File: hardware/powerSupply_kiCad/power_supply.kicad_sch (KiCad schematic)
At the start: 23 parts, among them IC1 LT7101EUHE-PBF, J1 CLCK, J2 MODE

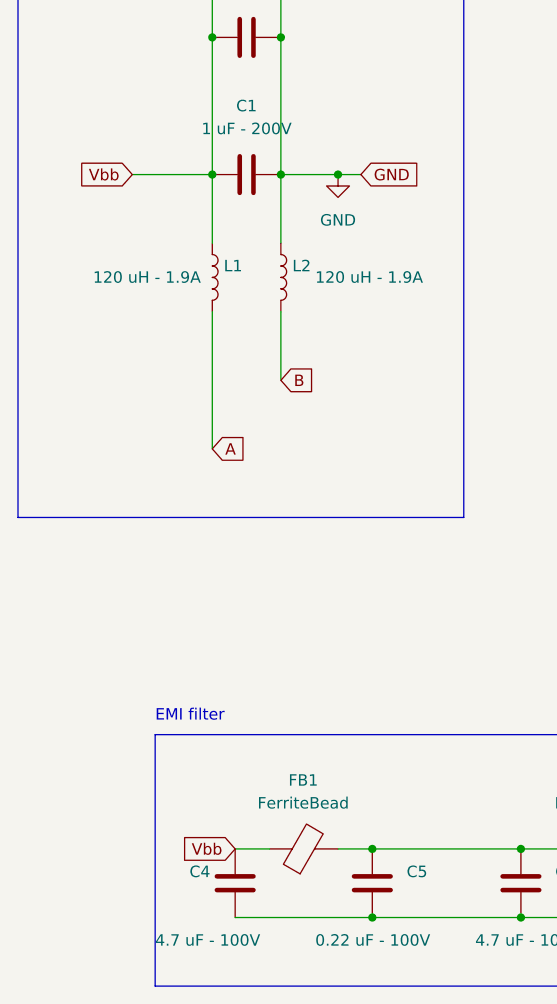
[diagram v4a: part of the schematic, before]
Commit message: Plane configuration
The Vin and Vbb are merged into a single net. Is the C1 to C3 usefull then? Must revise the decoupling strategy
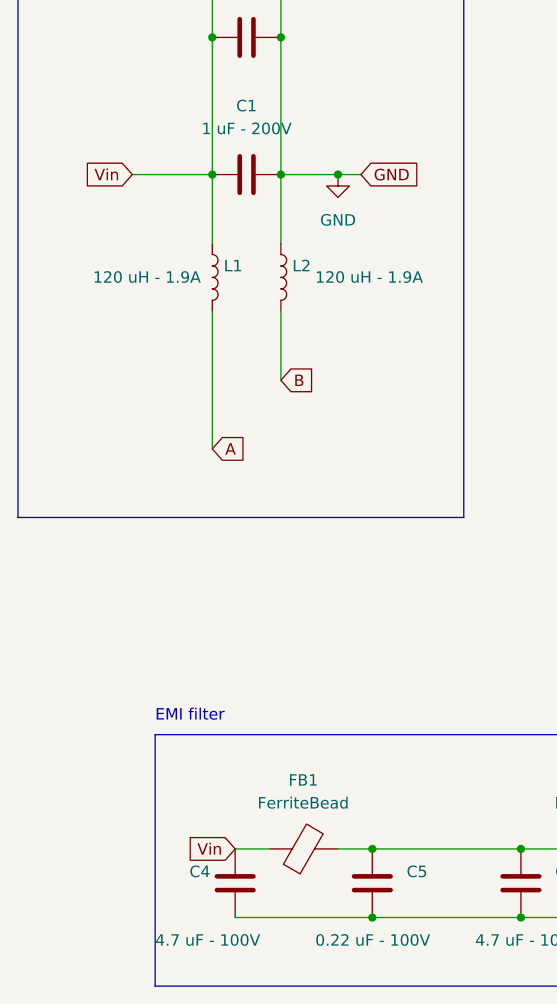
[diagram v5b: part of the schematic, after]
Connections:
- net Vbb is gone; now on net Vin: C1.1, C2.1, C3.1, C4.1, FB1.1, L1.1
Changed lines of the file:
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@@
     (effects (font (size 1.27 1.27)) (justify left bottom))
   )
-  (global_label "Vbb" (shape input) (at 53.34 154.94 180) (fields_autoplaced)
+  (global_label "Vin" (shape input) (at 53.34 154.94 180) (fields_autoplaced)
     (effects (font (size 1.27 1.27)) (justify right))
-    (property "Intersheet References" "${INTERSHEET_REFS}" (id 0) (at 47.5402 154.8606 0)
+    (property "Intersheet References" "${INTERSHEET_REFS}" (id 0) (at 48.0845 154.8606 0)
       (effects (font (size 1.27 1.27)) (justify right) hide)
     )
@@
     )
   )
-  (global_label "Vbb" (shape input) (at 41.91 80.01 180) (fields_autoplaced)
+  (global_label "Vin" (shape input) (at 41.91 80.01 180) (fields_autoplaced)
     (effects (font (size 1.27 1.27)) (justify right))
-    (property "Intersheet References" "${INTERSHEET_REFS}" (id 0) (at 36.1102 79.9306 0)
+    (property "Intersheet References" "${INTERSHEET_REFS}" (id 0) (at 36.6545 79.9306 0)
       (effects (font (size 1.27 1.27)) (justify right) hide)
     )

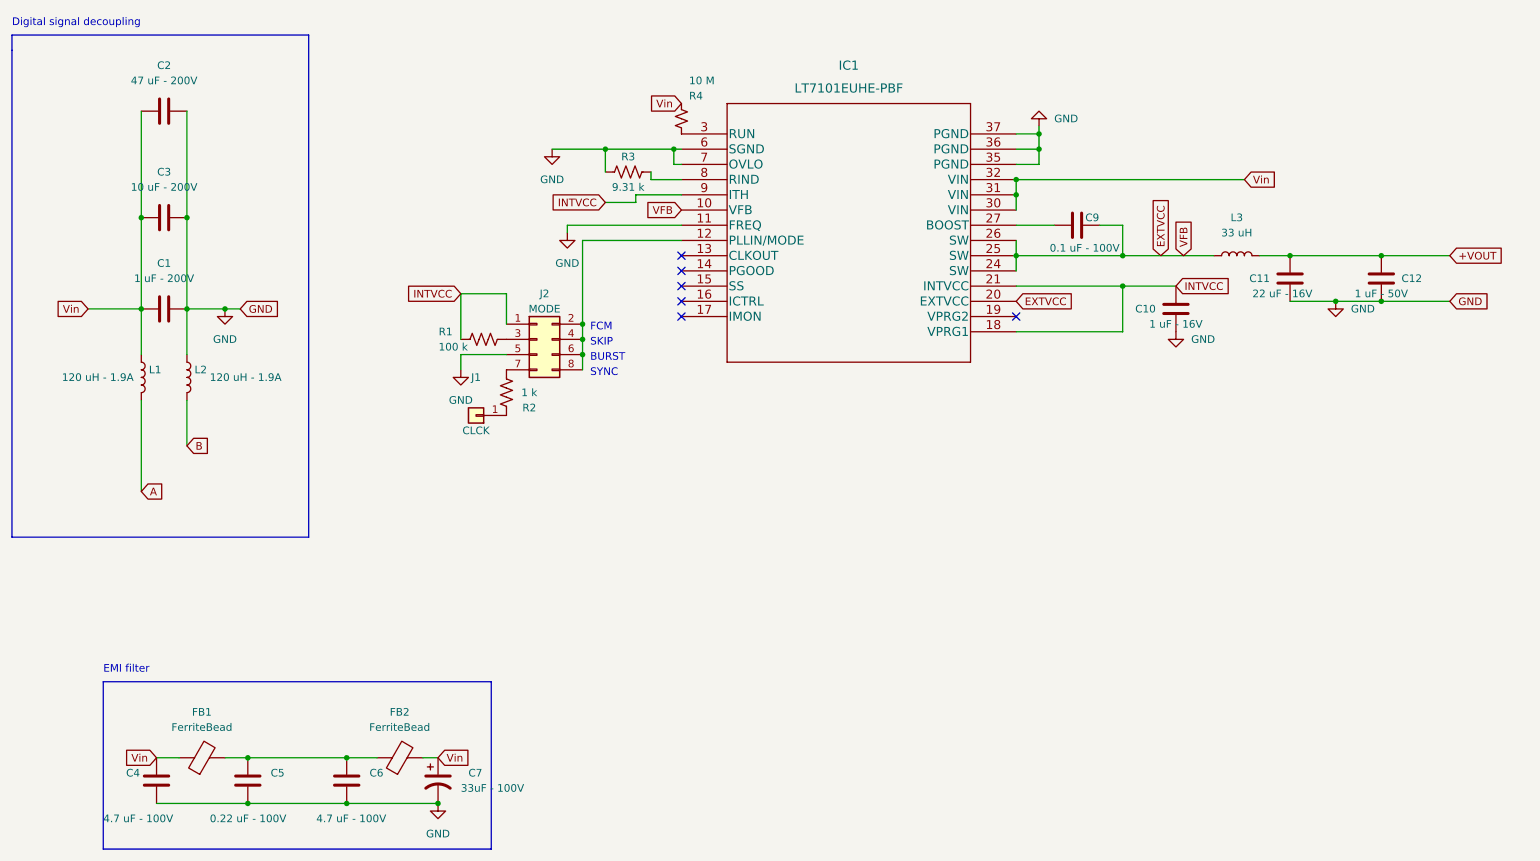
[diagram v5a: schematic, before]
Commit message: Finished connection and zone
The Vbb and Vin have returned to separate nets and zones. In this configuration the spike of volage when turning on the source at the surface will be handle by C1,C2 and C3.
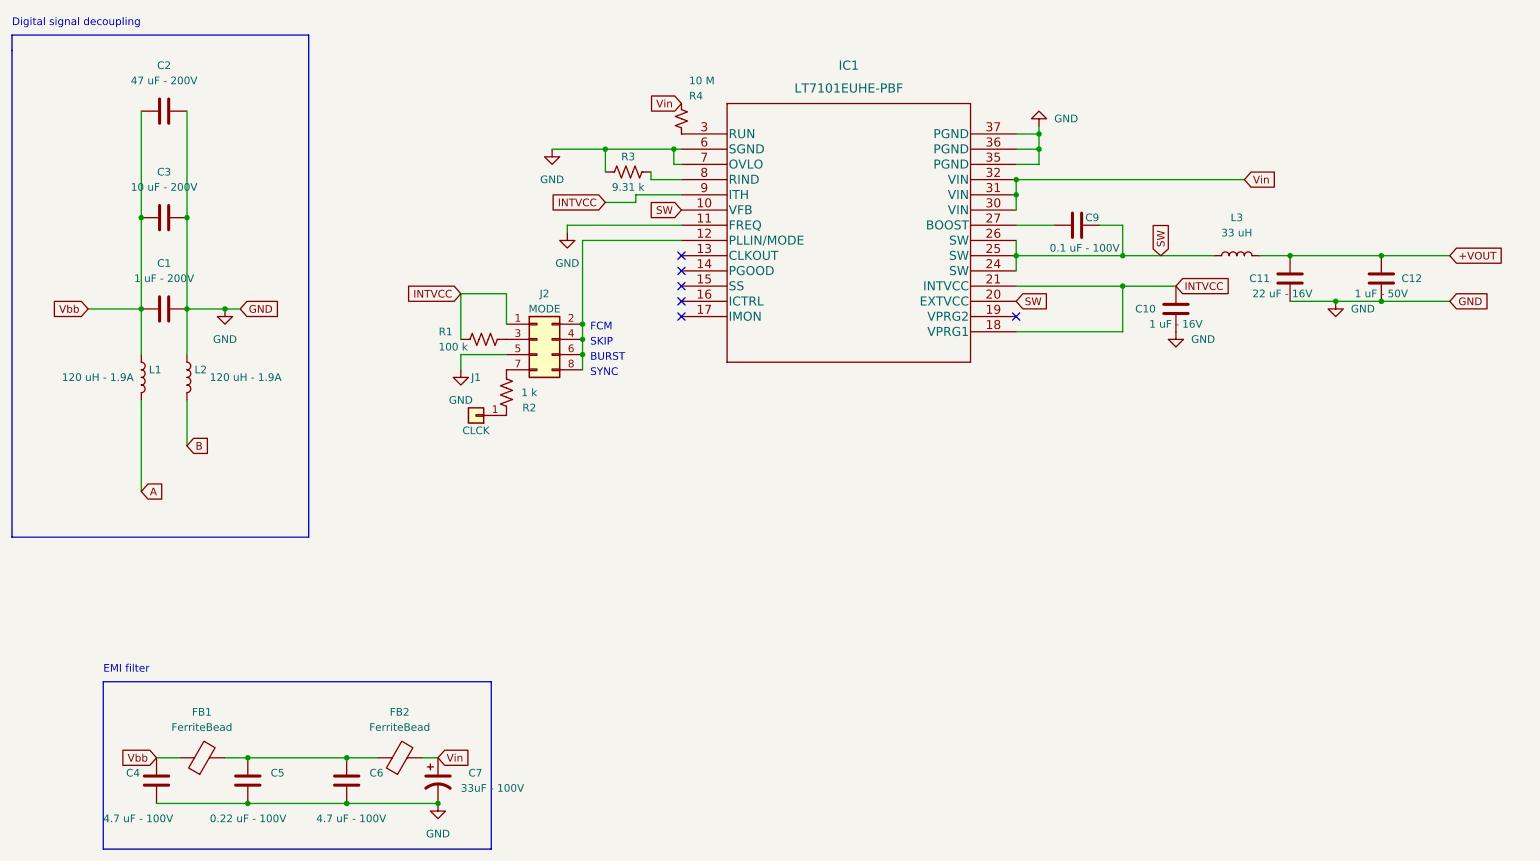
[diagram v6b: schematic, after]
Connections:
- net Vin: no longer C1.1, C2.1, C3.1, C4.1, FB1.1, L1.1
- net EXTVCC renamed SW
- new net Vbb: C1.1, C2.1, C3.1, C4.1, FB1.1, L1.1
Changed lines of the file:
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@@
     (effects (font (size 1.27 1.27)) (justify left bottom))
   )
-  (global_label "Vin" (shape input) (at 53.34 154.94 180) (fields_autoplaced)
+  (global_label "Vbb" (shape input) (at 53.34 154.94 180) (fields_autoplaced)
     (effects (font (size 1.27 1.27)) (justify right))
-    (property "Intersheet References" "${INTERSHEET_REFS}" (id 0) (at 48.0845 154.8606 0)
+    (property "Intersheet References" "${INTERSHEET_REFS}" (id 0) (at 47.5402 154.8606 0)
       (effects (font (size 1.27 1.27)) (justify right) hide)
     )
@@
     )
   )
-  (global_label "EXTVCC" (shape input) (at 196.85 78.74 0) (fields_autoplaced)
+  (global_label "SW" (shape input) (at 196.85 78.74 0) (fields_autoplaced)
     (effects (font (size 1.27 1.27)) (justify left))
-    (property "Intersheet References" "${INTERSHEET_REFS}" (id 0) (at 206.2179 78.6606 0)
+    (property "Intersheet References" "${INTERSHEET_REFS}" (id 0) (at 201.9241 78.6606 0)
       (effects (font (size 1.27 1.27)) (justify left) hide)
     )
@@
     (effects (font (size 1.27 1.27)) (justify left))
     (property "Intersheet References" "${INTERSHEET_REFS}" (id 0) (at 62.1031 102.7906 0)
-      (effects (font (size 1.27 1.27)) (justify left) hide)
-    )
-  )
-  (global_label "VFB" (shape input) (at 224.79 71.12 90) (fields_autoplaced)
-    (effects (font (size 1.27 1.27)) (justify left))
-    (property "Intersheet References" "${INTERSHEET_REFS}" (id 0) (at 224.8694 65.2598 90)
       (effects (font (size 1.27 1.27)) (justify left) hide)
     )
@@
     )
   )
-  (global_label "VFB" (shape input) (at 140.97 63.5 180) (fields_autoplaced)
+  (global_label "SW" (shape input) (at 140.97 63.5 180) (fields_autoplaced)
     (effects (font (size 1.27 1.27)) (justify right))
-    (property "Intersheet References" "${INTERSHEET_REFS}" (id 0) (at 135.1098 63.4206 0)
+    (property "Intersheet References" "${INTERSHEET_REFS}" (id 0) (at 135.8959 63.4206 0)
       (effects (font (size 1.27 1.27)) (justify right) hide)
     )
@@
     )
   )
-  (global_label "Vin" (shape input) (at 41.91 80.01 180) (fields_autoplaced)
+  (global_label "Vbb" (shape input) (at 41.91 80.01 180) (fields_autoplaced)
     (effects (font (size 1.27 1.27)) (justify right))
-    (property "Intersheet References" "${INTERSHEET_REFS}" (id 0) (at 36.6545 79.9306 0)
+    (property "Intersheet References" "${INTERSHEET_REFS}" (id 0) (at 36.1102 79.9306 0)
       (effects (font (size 1.27 1.27)) (justify right) hide)
     )
@@
     )
   )
-  (global_label "EXTVCC" (shape input) (at 220.98 71.12 90) (fields_autoplaced)
+  (global_label "SW" (shape input) (at 220.98 71.12 90) (fields_autoplaced)
     (effects (font (size 1.27 1.27)) (justify left))
-    (property "Intersheet References" "${INTERSHEET_REFS}" (id 0) (at 220.9006 61.7521 90)
+    (property "Intersheet References" "${INTERSHEET_REFS}" (id 0) (at 220.9006 66.0459 90)
       (effects (font (size 1.27 1.27)) (justify left) hide)
     )

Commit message: Place new molex connector on board
Molex 2 positions connector for 12V and A-B connections
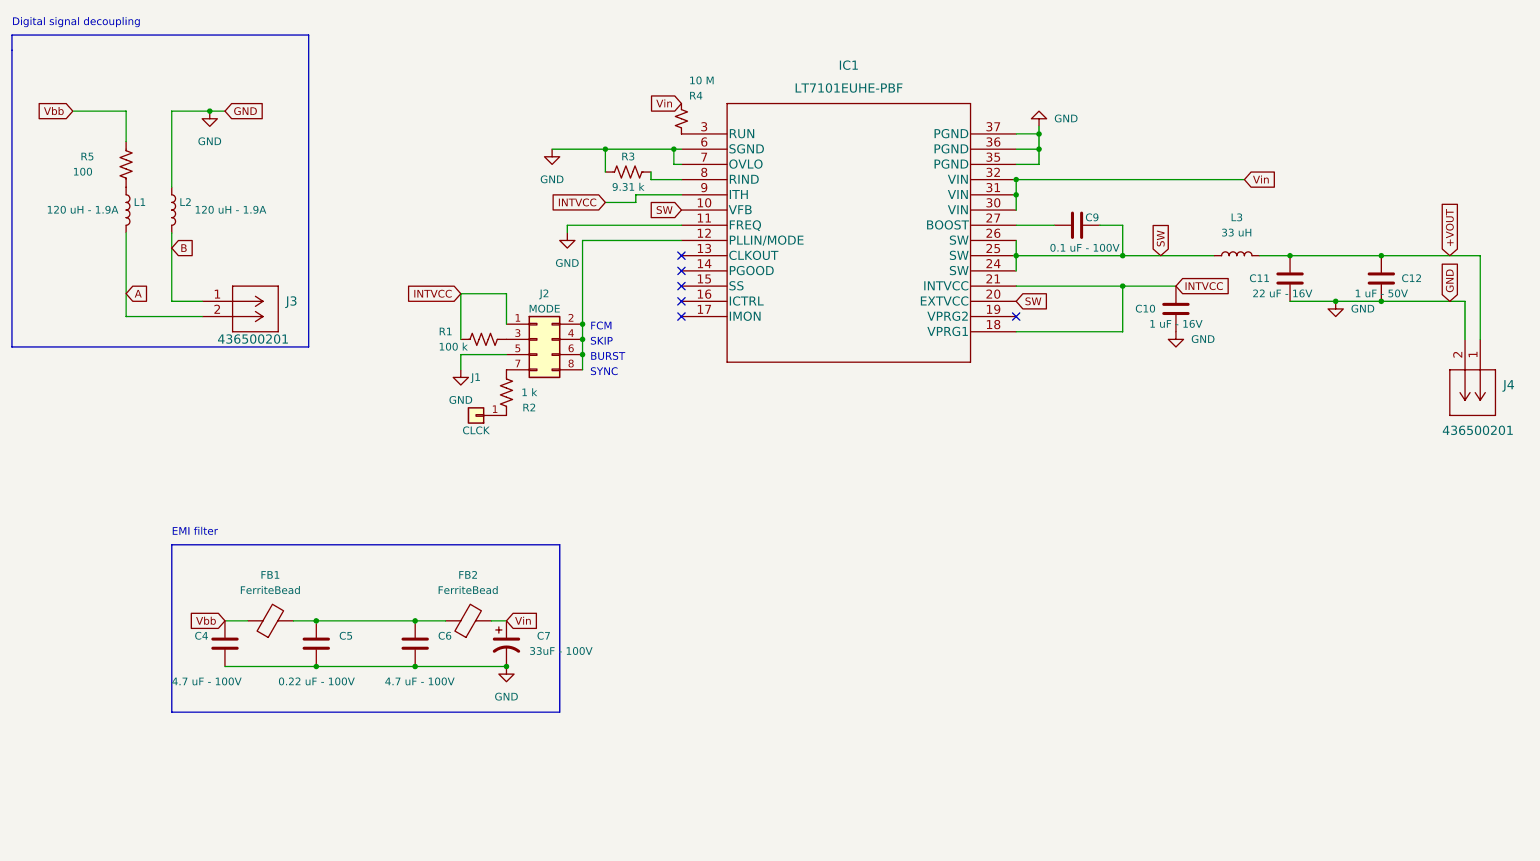
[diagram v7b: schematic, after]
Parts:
- removed C1: 1 uF - 200V, Capacitor_SMD:C_1812_4532Metric, symbol Device:C
- removed C2: 47 uF - 200V, Capacitor_THT:CP_Radial_D10.0mm_P5.00mm, symbol Device:C
- removed C3: 10 uF - 200V, Capacitor_THT:CP_Radial_D8.0mm_P3.50mm, symbol Device:C
- added J3, J4: 436500201, bib:436500201, symbol molex_2:436500201
- added R5: 100, Package_TO_SOT_THT:TO-220-2_Vertical, symbol Device:R_US
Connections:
- net +VOUT: now also J4.1
- net A: now also J3.2
- net B: now also J3.1
- net GND: now also J4.2
- net Vbb: now also R5.1; no longer L1.1
- new net: L1.1, R5.2
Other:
- moved on the sheet: C4, C5, C6, C7, FB1, FB2, L1, L2

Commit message: Added logo and board cutout
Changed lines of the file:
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@@
   (junction (at 257.81 71.12) (diameter 0) (color 0 0 0 0)
   )
+  (junction (at 200.66 53.34) (diameter 0) (color 0 0 0 0)
+  )
   (junction (at 214.63 76.2) (diameter 0) (color 0 0 0 0)
   )
@@
   )
   (junction (at 200.66 50.8) (diameter 0) (color 0 0 0 0)
-  )
-  (junction (at 200.66 53.34) (diameter 0) (color 0 0 0 0)
   )
   (junction (at 250.19 78.74) (diameter 0) (color 0 0 0 0)
@@
     (stroke (width 0) (type default) (color 0 0 0 0))
   )
+  (wire (pts (xy 200.66 50.8) (xy 200.66 53.34))
+    (stroke (width 0) (type default) (color 0 0 0 0))
+  )
   (wire (pts (xy 237.49 71.12) (xy 242.57 71.12))
     (stroke (width 0) (type default) (color 0 0 0 0))
@@
     (stroke (width 0) (type default) (color 0 0 0 0))
   )
+  (wire (pts (xy 200.66 53.34) (xy 200.66 55.88))
+    (stroke (width 0) (type default) (color 0 0 0 0))
+  )
   (polyline (pts (xy 78.74 86.36) (xy 78.74 34.29))
     (stroke (width 0) (type default) (color 0 0 0 0))
@@
     (stroke (width 0) (type default) (color 0 0 0 0))
   )
-  (wire (pts (xy 200.66 55.88) (xy 200.66 53.34))
-    (stroke (width 0) (type default) (color 0 0 0 0))
-  )
   (polyline (pts (xy 55.88 119.38) (xy 55.88 147.32))
     (stroke (width 0) (type default) (color 0 0 0 0))
@@
     (stroke (width 0) (type default) (color 0 0 0 0))
   )
-  (wire (pts (xy 200.66 53.34) (xy 200.66 50.8))
-    (stroke (width 0) (type default) (color 0 0 0 0))
-  )
